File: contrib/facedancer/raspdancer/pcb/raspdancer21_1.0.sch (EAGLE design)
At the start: 15 parts, among them Q1 12Mhz

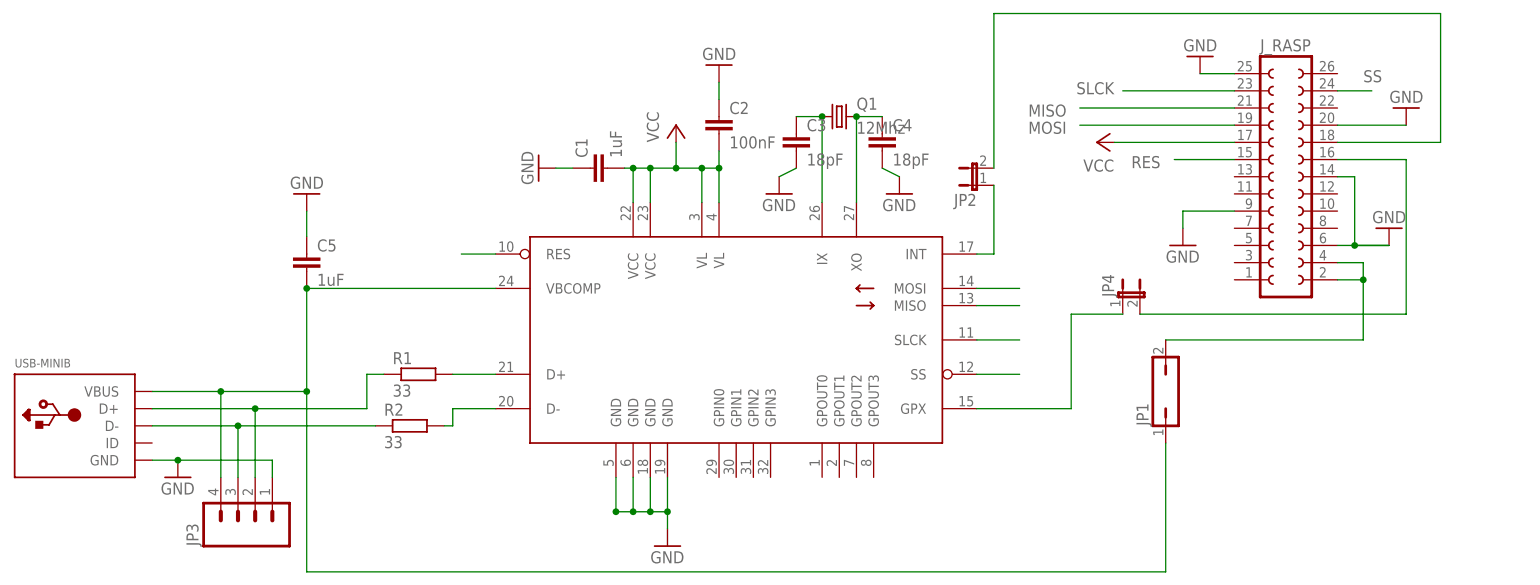
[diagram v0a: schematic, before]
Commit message: Add raspdancer21 sch & brd
git-svn-id: https://svn.code.sf.net/p/goodfet/code@1588 12e2690d-a6be-4b82-a7b7-67c4a43b65c8
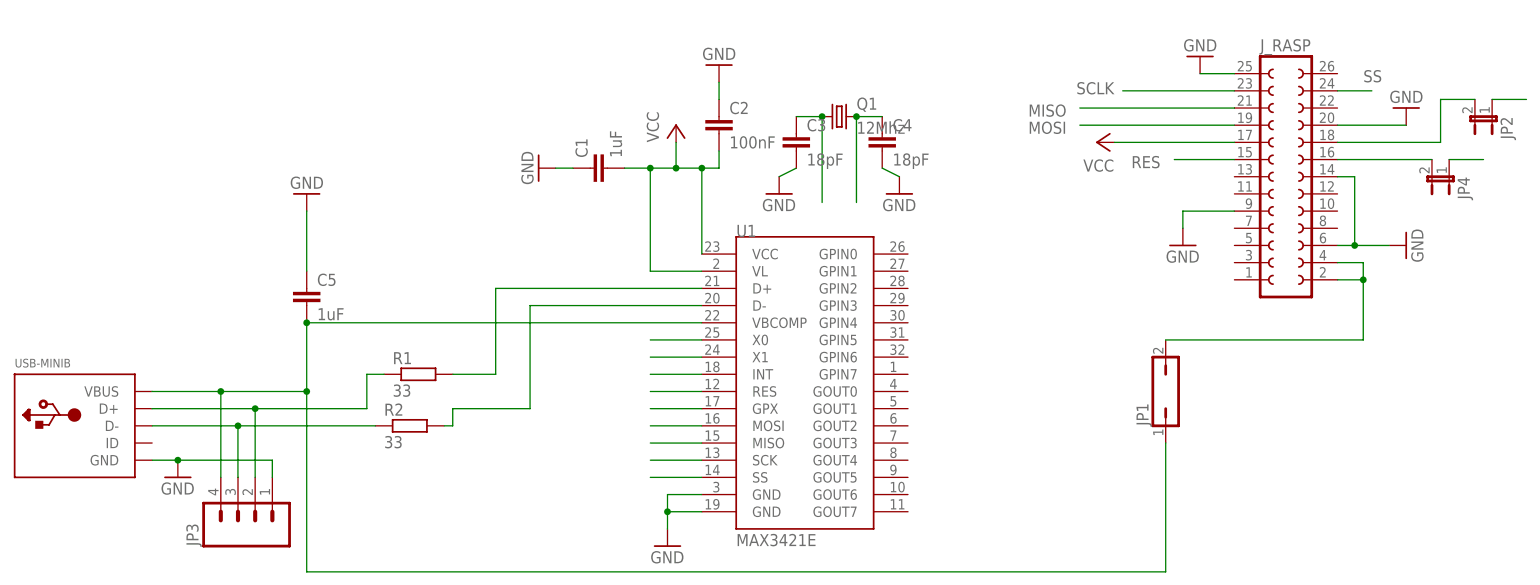
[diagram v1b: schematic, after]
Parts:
- U1: value (none) -> MAX3421E; device maxim-2:MAX3420 -> SparkFun-DigitalIC:MAX3421ESMD
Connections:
- net VBUS renamed VBCOMP
- removed net SLCK: J_RASP.23, U1.SLCK
- new net SCLK: J_RASP.23, U1.SCK
- net GND: now also U1.GND@19; no longer U1.GND@1, U1.GND@2, U1.GND@4
- net IX: now also C4.1, Q1.2, U1.X0; no longer C3.1, Q1.1, U1.IX
- net VCC: now also U1.VCC, U1.VL; no longer U1.VCC@1, U1.VCC@2, U1.VL@1, U1.VL@2
- net XO: now also C3.1, Q1.1, U1.X1; no longer C4.1, Q1.2, U1.XO
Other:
- moved on the sheet: C5, JP2, JP4

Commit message: raspdancer pcb edited
thanks to Zac Franken for his tuning tips

git-svn-id: https://svn.code.sf.net/p/goodfet/code@1589 12e2690d-a6be-4b82-a7b7-67c4a43b65c8
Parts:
- removed C5: 1uF, 00_mylib:C1206
- removed JP3: (no value), SparkFun:M04PTH
- added JP5: USB-A-S, SparkFun-Connectors:USB-A-S
- J_RASP: device con-lsta:FE13-2 -> doegox:FE13-2
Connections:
- removed net VBCOMP: C5.2, JP1.1, JP3.4, U1.VBCOMP, USB-MINIB.VBUS
- new net VBUS: C1.2, JP1.1, JP5.VBUS, U1.VBCOMP, USB-MINIB.VBUS
- net D+2: now also JP5.D+; no longer JP3.2
- net D-2: now also JP5.D-; no longer JP3.3
- net GND: now also JP5.GND, USB-MINIB.GND; no longer C5.1, JP3.1
- net VCC: no longer C1.2
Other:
- moved on the sheet: C1, C2, C3, C4, Q1

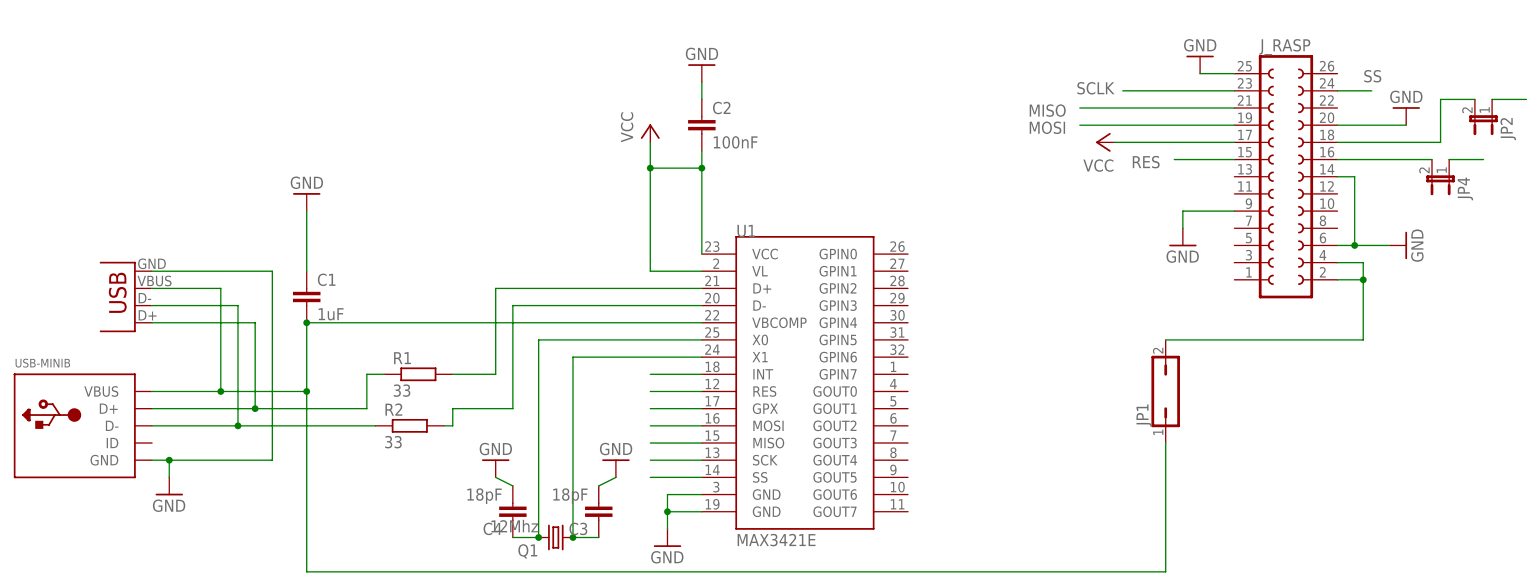
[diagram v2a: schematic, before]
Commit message: raspdancer21: fix silkscreen
git-svn-id: https://svn.code.sf.net/p/goodfet/code@1590 12e2690d-a6be-4b82-a7b7-67c4a43b65c8
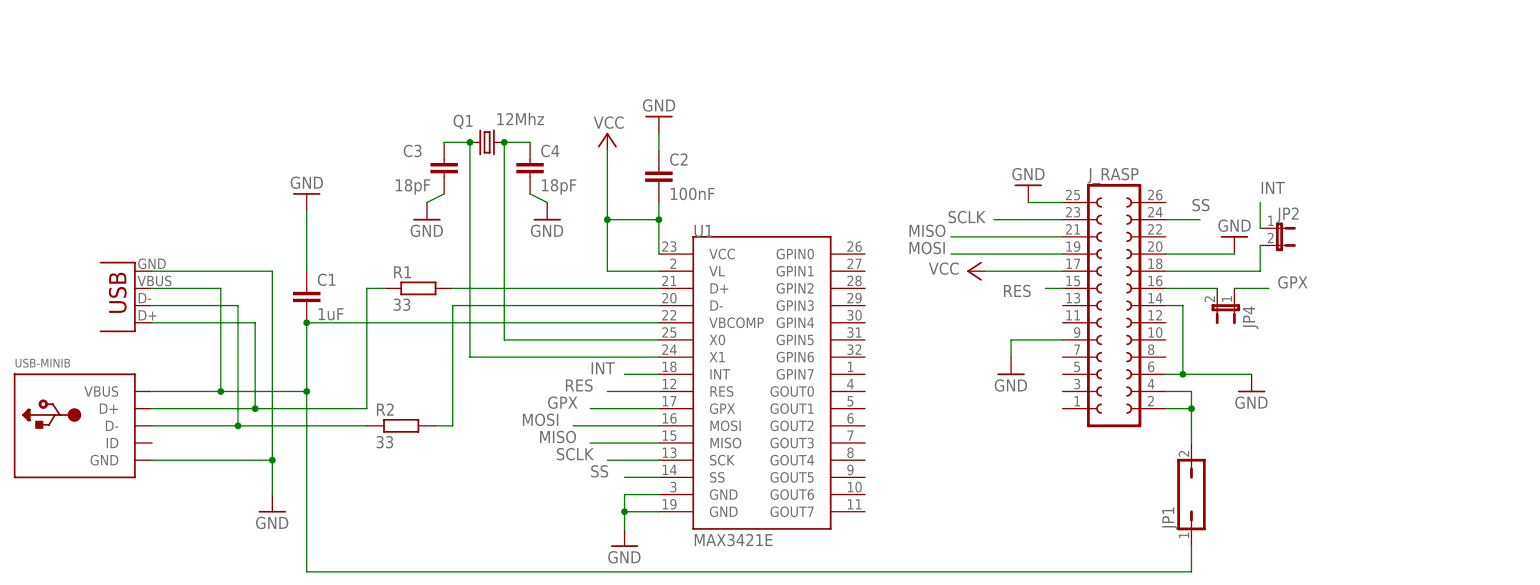
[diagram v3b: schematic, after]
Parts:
- renumbered JP5 to USB-A
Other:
- moved on the sheet: C2, C3, C4, JP1, JP2, JP4, J_RASP, Q1, R1, R2, U1
